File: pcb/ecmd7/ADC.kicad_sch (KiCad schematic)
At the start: 13 parts, among them U2 MAX11049ETN+

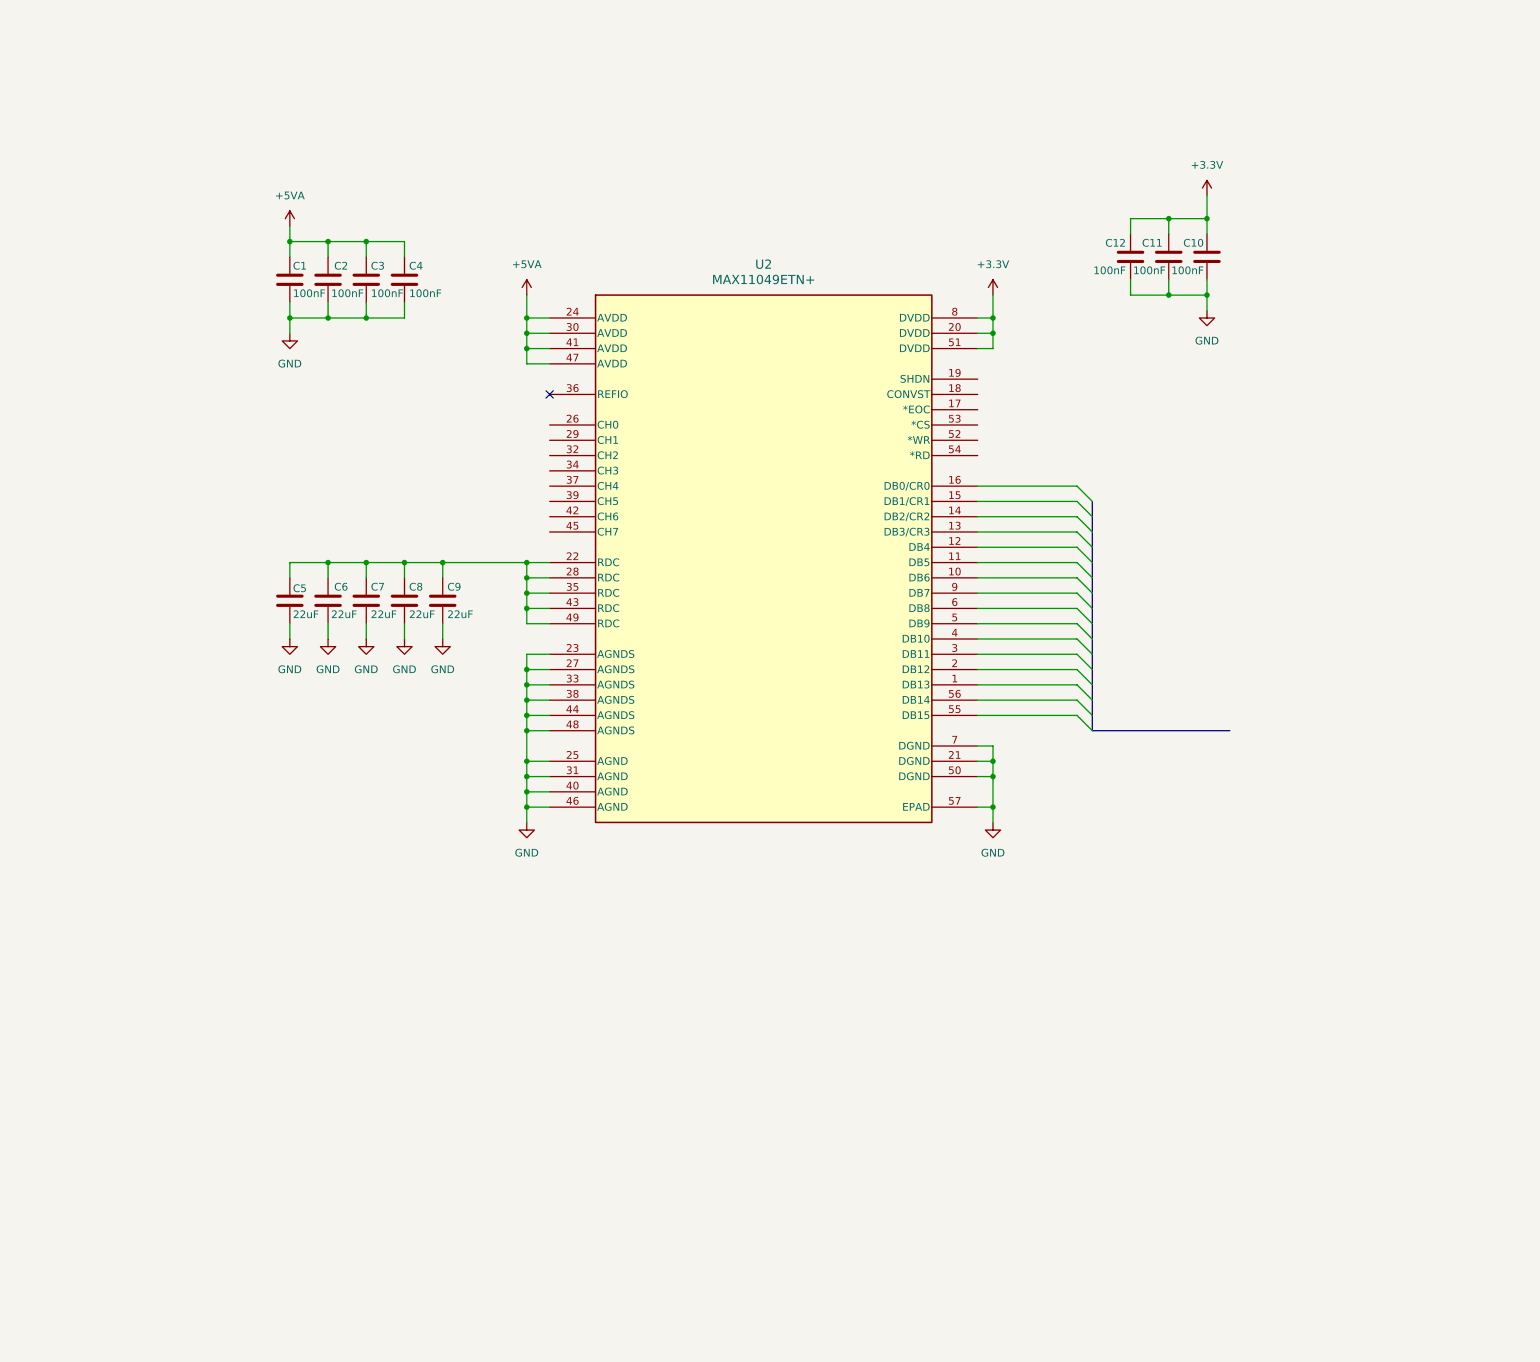
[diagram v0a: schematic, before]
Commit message: WIP: Add ADC inputs
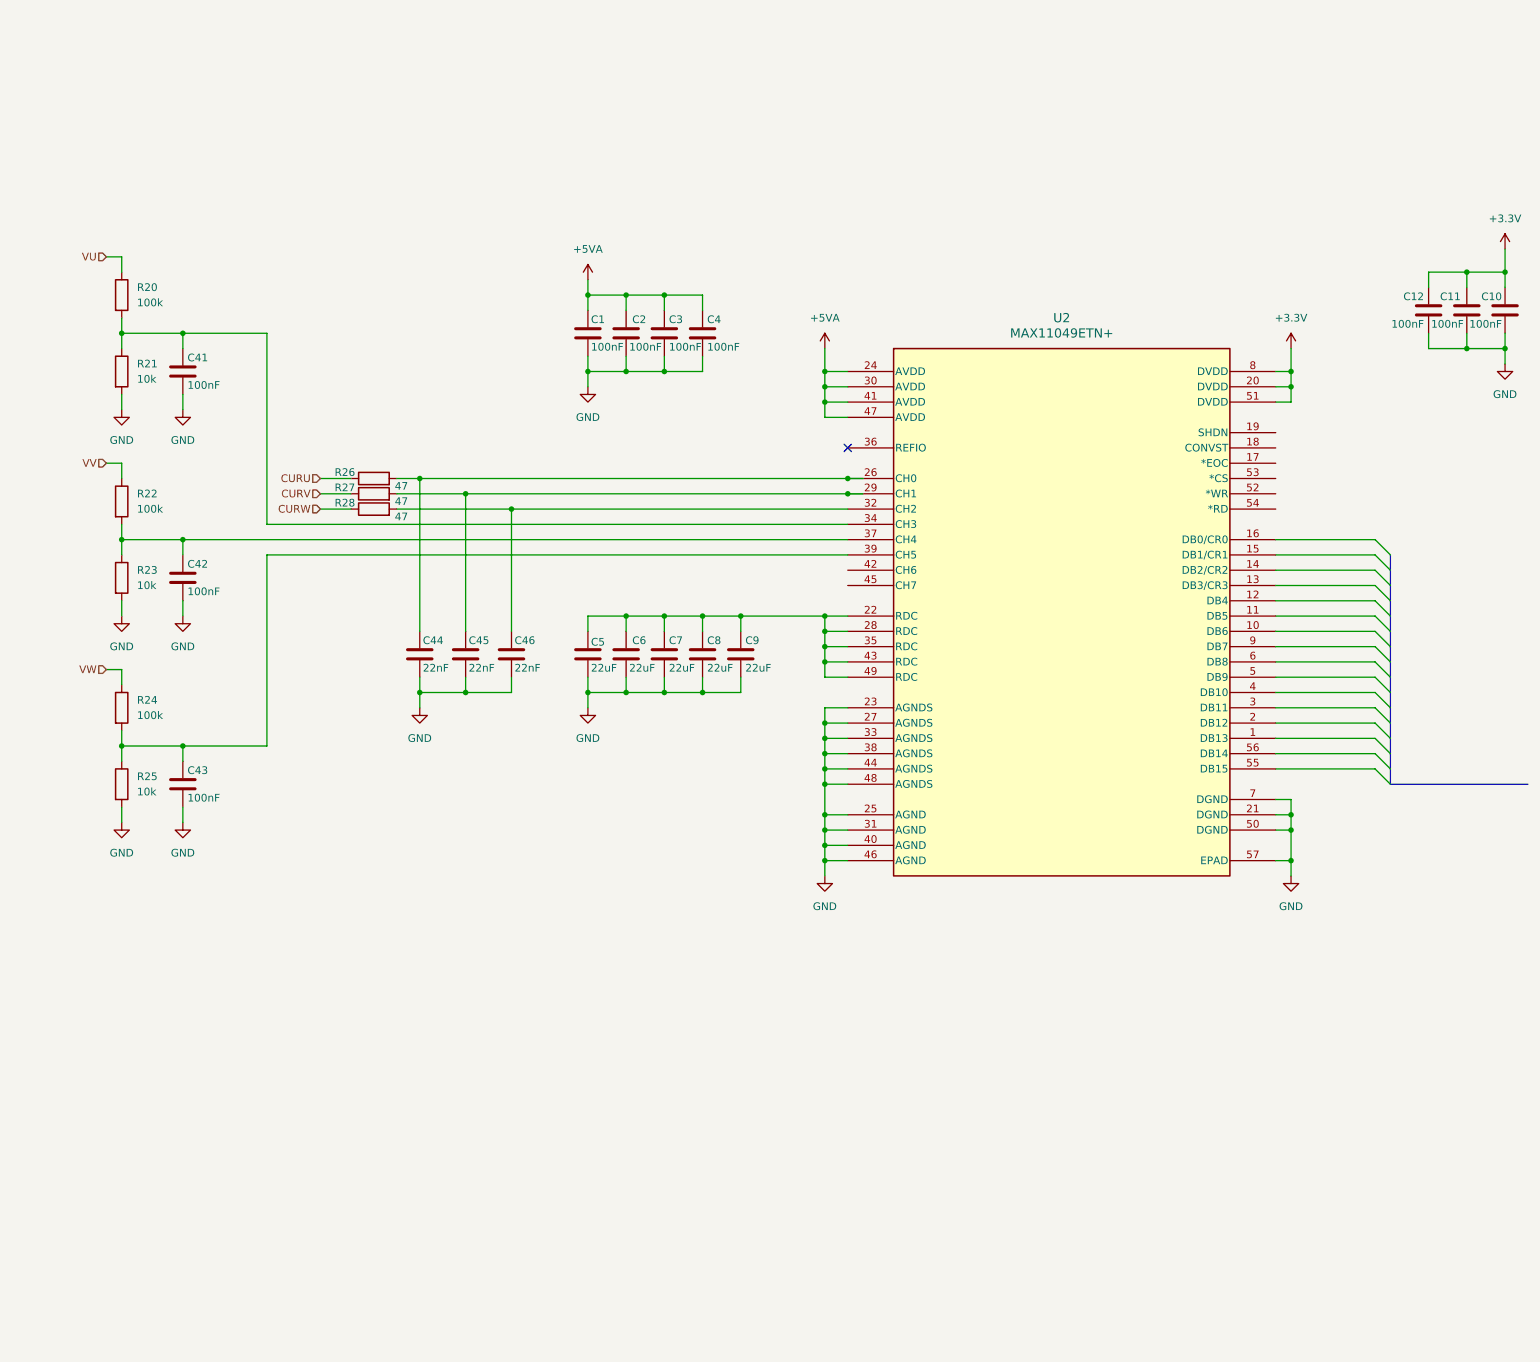
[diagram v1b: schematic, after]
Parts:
- added C41, C42, C43: 100nF, symbol Device:C
- added C44, C45, C46: 22nF, symbol Device:C
- added R20, R22, R24: 100k, Resistor_SMD:R_0805_2012Metric, symbol Device:R
- added R21, R23, R25: 10k, Resistor_SMD:R_0805_2012Metric, symbol Device:R
- added R26, R27, R28: 47, Resistor_SMD:R_0805_2012Metric, symbol Device:R
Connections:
- net GND: now also C41.2, C42.2, C43.2, C44.2, C45.2, C46.2, R21.2, R23.2, R25.2
- net at U2.26 (CH0): now also C44.1, R26.2
- net at U2.29 (CH1): now also C45.1, R27.2
- net at U2.32 (CH2): now also C46.1, R28.2
- net at U2.34 (CH3): now also C41.1, R20.2, R21.1
- net at U2.37 (CH4): now also C42.1, R22.2, R23.1
- net at U2.39 (CH5): now also C43.1, R24.2, R25.1
- new net CURU: R26.1
- new net CURV: R27.1
- new net CURW: R28.1
- new net VU: R20.1
- new net VV: R22.1
- new net VW: R24.1
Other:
- moved on the sheet: C1, C10, C11, C12, C2, C3, C4, C5, C6, C7, C8, C9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

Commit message: WIP: Update ADC schematic with cheaper solution
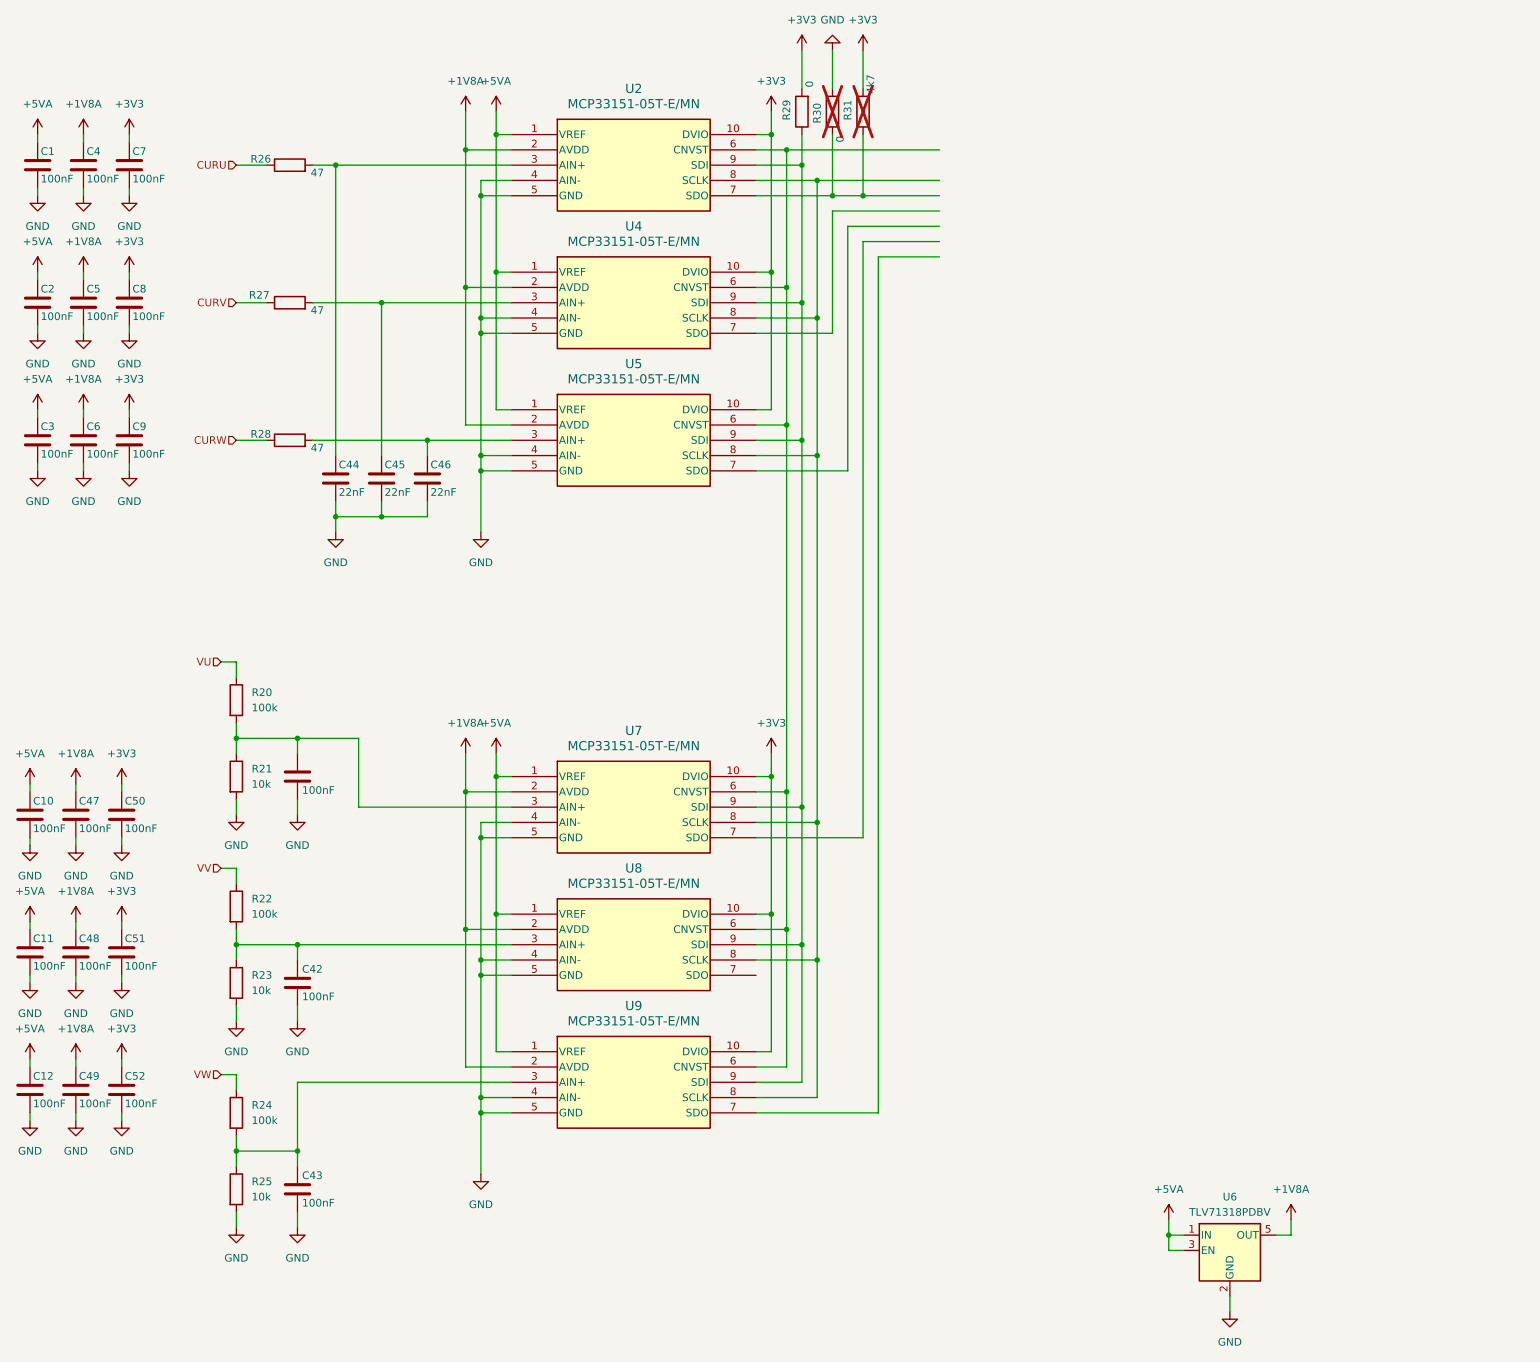
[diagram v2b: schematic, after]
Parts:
- removed U2: MAX11049ETN+, 21-0135F_T5688-3_MXM, symbol ssta_symbols:MAX11049ETN+
- added C47, C48, C49, C50, C51, C52: 100nF, symbol Device:C
- added R29, R30: 0, Resistor_SMD:R_0805_2012Metric, symbol Device:R
- added R31: 4k7, Resistor_SMD:R_0805_2012Metric, symbol Device:R
- added U2, U4, U5, U7, U8, U9: MCP33151-05T-E/MN, TDFN10_MN_MCH, symbol ssta_symbols:MCP33151-05T-E_MN
- added U6: TLV71318PDBV, Package_TO_SOT_SMD:SOT-23-5, symbol Regulator_Linear:TLV71318PDBV
- C5, C6, C7, C8, C9: value 22uF -> 100nF
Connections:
- net +3.3V is gone; now on net +5VA: C10.1, C11.1, C12.1
- net +5VA: now also U2.1 (VREF), U4.1 (VREF), U5.1 (VREF), U6.1 (IN), U6.3 (EN), U7.1 (VREF), U8.1 (VREF), U9.1 (VREF); no longer C4.1
- net GND: now also C47.2, C48.2, C49.2, C50.2, C51.2, C52.2, R30.1, U2.4 (AIN-), U2.5 (GND), U4.4 (AIN-), U4.5 (GND), U5.4 (AIN-), U5.5 (GND), U6.2 (GND), U7.4 (AIN-), U7.5 (GND), U8.4 (AIN-), U8.5 (GND), U9.4 (AIN-), U9.5 (GND)
- net at C44.1, R26.2: now also U2.3 (AIN+)
- net at C45.1, R27.2: now also U4.3 (AIN+)
- net +3V3: now reaches C7.1, C8.1, C9.1
- net +3V3: now also C50.1, C51.1, C52.1, R29.2, R31.2, U2.10 (DVIO), U4.10 (DVIO), U5.10 (DVIO), U7.10 (DVIO), U8.10 (DVIO), U9.10 (DVIO); no longer C5.1, C6.1
- net at C41.1, R20.2, R21.1: now also U7.3 (AIN+)
- net at C42.1, R22.2, R23.1: now also U8.3 (AIN+)
- net at C46.1, R28.2: now also U5.3 (AIN+)
- net at C43.1, R24.2, R25.1: now also U9.3 (AIN+)
- new net: R30.2, R31.1, U2.7 (SDO)
- new net: U2.6 (CNVST), U4.6 (CNVST), U5.6 (CNVST), U7.6 (CNVST), U8.6 (CNVST), U9.6 (CNVST)
- new net: U2.8 (SCLK), U4.8 (SCLK), U5.8 (SCLK), U7.8 (SCLK), U8.8 (SCLK), U9.8 (SCLK)
- new net: R29.1, U2.9 (SDI), U4.9 (SDI), U5.9 (SDI), U7.9 (SDI), U8.9 (SDI), U9.9 (SDI)
- new net +1V8A: C4.1, C47.1, C48.1, C49.1, C5.1, C6.1, U2.2 (AVDD), U4.2 (AVDD), U5.2 (AVDD), U6.5 (OUT), U7.2 (AVDD), U8.2 (AVDD), U9.2 (AVDD)
- no-connect marks 1 -> 0
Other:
- moved on the sheet: C1, C42, C43, C44, C45, C46, R20, R21, R22, R23, R24, R25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
